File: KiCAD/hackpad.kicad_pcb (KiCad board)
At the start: 2 copper layers, 5 parts, among them SW1 SW_Push, SW2 SW_Push, SW3 SW_Push, U1 XIAO-SAMD21-SMD

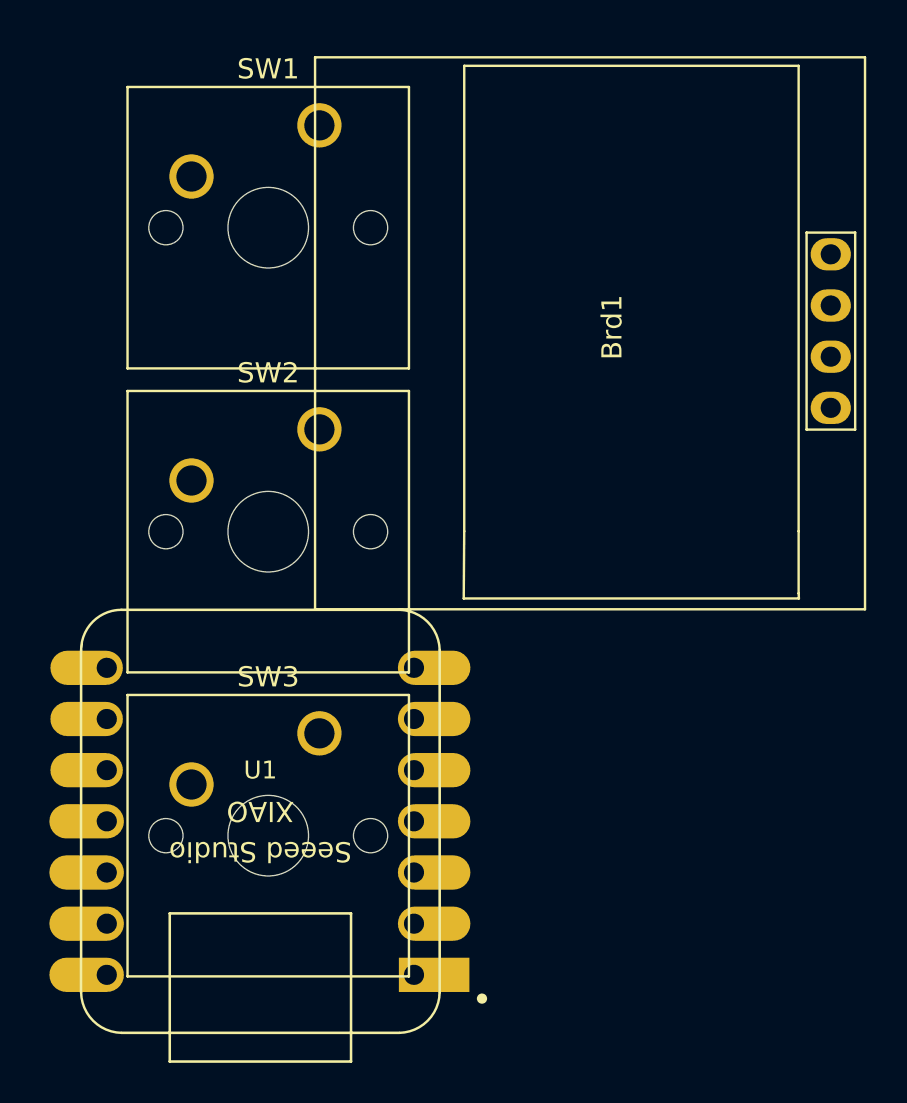
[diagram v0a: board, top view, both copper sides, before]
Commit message: Updated the KiCad files to include the screen
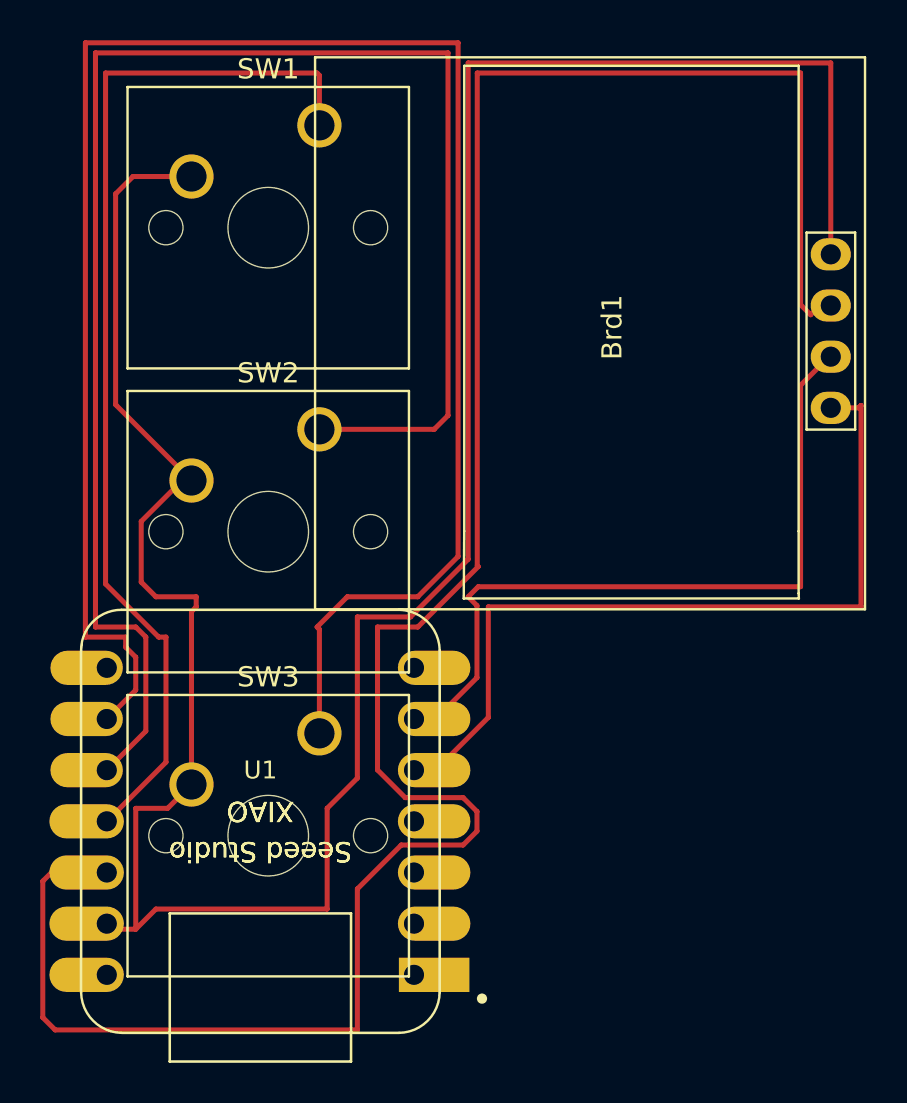
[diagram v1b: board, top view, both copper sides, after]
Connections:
- Brd1 pad 1: Net-(Brd1-GND) -> GND
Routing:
- net GND: track 0.00 -> 133.4 mm
- net Net-(Brd1-VCC): track 0.00 -> 114.2 mm
- net Net-(U1-PA7_A8_D8_SCK): track 0.00 -> 94.1 mm
- net Net-(U1-PA5_A9_D9_MISO): track 0.00 -> 80.8 mm
- net Net-(U1-PA6_A10_D10_MOSI): track 0.00 -> 53.0 mm
- net Net-(Brd1-SDA): track 0.00 -> 40.3 mm
- net Net-(Brd1-SCL): track 0.00 -> 37.0 mm
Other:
- board text added: "Seeed Studio"
- board text added: "XIAO"
